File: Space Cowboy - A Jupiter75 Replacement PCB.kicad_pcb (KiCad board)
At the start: 2 copper layers, 313.5 x 129.5 mm, 237 parts, among them SW1 SW_PUSH, U1 ATmega32U4-AU, Y1 16MHz

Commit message: Update Space Cowboy - A Jupiter75 Replacement PCB.kicad_pcb
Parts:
- moved CRGB12 137.7 mm to (14.1, 43.7)
- moved CRGB6 119.2 mm to (161.1, 177.2)
- moved DRGB1 73.8 mm to (-24.5, 88.1)
- moved CRGB1 69.6 mm to (8.48, 49.6)
- moved CRGB2 62.9 mm to (-12.9, 54.4)
- moved DRGB17 61.6 mm to (92.9, 173.8)
- moved DRGB2 58.8 mm to (-11.5, 45.6)
- moved DRGB18 49.5 mm to (-2.03, 155.2)
- moved CRGB18 44.8 mm to (5.18, 153.3)
- moved DRGB9 37.3 mm to (321.4, 23.7)
- moved CRGB9 34.9 mm to (327.8, 20.7)
- moved DRGB11 31.7 mm to (379.3, 167.1)
- moved CRGB11 28.8 mm to (373.8, 162.9)
- moved DRGB10 23.2 mm to (371.3, 103.5)
- moved CRGB10 20.2 mm to (370.7, 111.8)
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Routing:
- net (no net): track 50.4 -> 0.00 mm
- net ROW5: track 272.3 -> 321.1 mm
- net +5V: track 294.4 -> 265.2 mm
- net GND: track 92.6 -> 68.7 mm
- net Net-(F1-Pad2): track 12.2 -> 4.56 mm
- net D+: track 21.7 -> 15.6 mm
- net D-: track 21.1 -> 15.4 mm
- net ROW4: track 278.7 -> 283.3 mm
- net Net-(R2-Pad2): track 192.5 -> 188.4 mm
- net Net-(R3-Pad1): track 193.2 -> 189.3 mm
- net Net-(D80-Pad2): track 28.8 -> 26.8 mm
- net Net-(R5-Pad1): track 3.84 -> 5.76 mm
- net Net-(FB2-Pad2): track 33.9 -> 35.4 mm
- net VBUS: track 20.2 -> 18.9 mm
- net COL0: track 152.5 -> 151.9 mm
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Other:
- board size 313.5 x 129.5 mm -> 303.5 x 119.5 mm

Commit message: Update Space Cowboy - A Jupiter75 Replacement PCB.kicad_pcb
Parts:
- moved D83 10.1 mm to (312.8, 152.4)
- moved D81 10.1 mm to (258.0, 152.4)
- moved D84 10.0 mm to (331.7, 152.4)
- moved D82 7.14 mm to (281.8, 152.4)
- moved D80 6.12 mm to (196.8, 146.3), turned to 270 degrees
- moved R7 3.71 mm to (138.7, 145.9)
- moved C3 3.57 mm to (157.2, 148.1)
- moved C1 3.56 mm to (142.0, 151.0)
- moved C4 3.51 mm to (142.0, 149.7)
- moved R1 3.43 mm to (158.5, 154.4)
- moved Y1 3.39 mm to (149.9, 141.0)
- moved U1 3.38 mm to (150.1, 151.2)
- moved D85 3.20 mm to (341.9, 156.5), turned to 0 degrees
- moved C6 3.01 mm to (153.3, 141.4)
- moved C7 3.01 mm to (146.4, 141.4)
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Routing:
- net ROW5: track 321.1 -> 290.0 mm
- net Net-(R2-Pad2): track 188.4 -> 173.6 mm
- net Net-(R3-Pad1): track 189.3 -> 174.7 mm
- net +5V: track 265.2 -> 268.7 mm
- net Net-(D85-Pad2): track 11.4 -> 9.31 mm
- net GND: track 68.7 -> 66.7 mm
- net Net-(D80-Pad2): track 26.8 -> 25.6 mm
- net Net-(D84-Pad2): track 10.8 -> 9.64 mm
- net Net-(D81-Pad2): track 10.8 -> 9.75 mm
- net Net-(D83-Pad2): track 10.8 -> 9.79 mm

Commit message: Update Space Cowboy - A Jupiter75 Replacement PCB.kicad_pcb
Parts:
- moved DRGB18 143.9 mm to (141.0, 139.4), turned to 180 degrees
- moved DRGB1 137.5 mm to (103.0, 139.4), turned to 180 degrees
- moved DRGB2 121.1 mm to (65.0, 139.4), turned to 135 degrees
- moved DRGB17 92.8 mm to (179.0, 139.4), turned to 180 degrees
- moved DRGB14 66.7 mm to (293.0, 139.4), turned to 180 degrees
- moved DRGB15 64.1 mm to (255.0, 139.4), turned to 180 degrees
- moved DRGB13 63.1 mm to (331.1, 139.4), turned to 225 degrees
- moved DRGB16 56.9 mm to (217.0, 139.4), turned to 180 degrees
- moved C6 20.0 mm to (134.4, 148.0), turned to 0 degrees
- moved Y1 18.7 mm to (134.3, 151.4), turned to 270 degrees
- moved C7 18.0 mm to (134.4, 154.8), turned to 0 degrees
- moved C8 16.6 mm to (136.5, 158.2), turned to 90 degrees
- moved C5 16.3 mm to (162.2, 154.8), turned to 270 degrees
- moved R7 14.1 mm to (142.2, 159.6), turned to 90 degrees
- moved C2 13.4 mm to (162.2, 147.5), turned to 270 degrees
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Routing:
- net +5V: track 268.7 -> 179.1 mm, vias 7 -> 2
- net GND: track 66.7 -> 9.08 mm, vias 2 -> 0
- net Net-(C7-Pad1): track 12.2 -> 0.82 mm
- net ROW4: track 283.3 -> 276.4 mm
- net Net-(C6-Pad2): track 8.79 -> 14.7 mm
- net ROW5: track 290.0 -> 284.3 mm
- net Net-(R1-Pad1): track 5.08 -> 0.00 mm
- net Net-(D70-Pad2): track 10.8 -> 13.1 mm
- net Net-(D68-Pad2): track 10.8 -> 13.1 mm
- net Net-(D64-Pad2): track 10.8 -> 13.1 mm
- net Net-(D72-Pad2): track 10.8 -> 13.1 mm
- net Net-(D66-Pad2): track 10.8 -> 13.0 mm
- net Net-(R7-Pad2): track 8.93 -> 6.99 mm
- net Net-(D63-Pad2): track 13.1 -> 11.5 mm

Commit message: Update Space Cowboy - A Jupiter75 Replacement PCB.kicad_pcb
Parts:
- moved CRGB13 332.8 mm to (328.4, 136.8), turned to 45 degrees
- moved CRGB12 323.4 mm to (331.0, 108.5), turned to 180 degrees
- moved CRGB14 301.2 mm to (291.9, 135.6)
- moved CRGB15 254.2 mm to (255.0, 135.7)
- moved CRGB16 221.5 mm to (217.0, 135.7)
- moved CRGB8 213.0 mm to (217.0, 73.8), turned to 180 degrees
- moved CRGB17 188.4 mm to (179.0, 135.7)
- moved CRGB7 178.4 mm to (179.1, 73.8), turned to 180 degrees
- moved CRGB4 144.9 mm to (62.4, 67.5), turned to 225 degrees
- moved CRGB18 137.0 mm to (141.0, 135.7), turned to 0 degrees
- moved CRGB1 127.9 mm to (103.0, 135.7), turned to 0 degrees
- moved CRGB5 125.4 mm to (103.0, 73.8), turned to 180 degrees
- moved CRGB2 115.6 mm to (62.4, 142.1), turned to 315 degrees
- moved DRGB11 108.4 mm to (331.0, 70.1), turned to 315 degrees
- moved CRGB6 105.4 mm to (141.1, 73.8), turned to 180 degrees
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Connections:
- DRGB1 pad 4DIN: (no net) -> RGB_DI_PIN
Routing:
- net +5V: track 179.1 -> 1045.2 mm, vias 2 -> 8
- net (no net): track 0.00 -> 588.0 mm, vias 0 -> 8
- net GND: track 9.08 -> 66.7 mm
- net ROW2: track 282.6 -> 276.8 mm
- net Net-(D33-Pad2): track 10.8 -> 15.2 mm
- net COL2: track 121.7 -> 123.8 mm
- net Net-(D46-Pad2): track 5.14 -> 3.70 mm

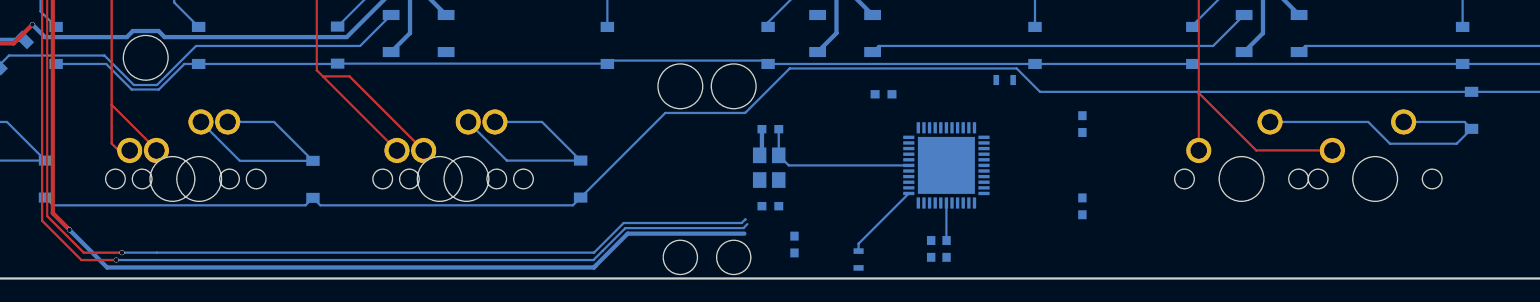
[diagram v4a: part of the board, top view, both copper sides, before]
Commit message: Update Space Cowboy - A Jupiter75 Replacement PCB.kicad_pcb
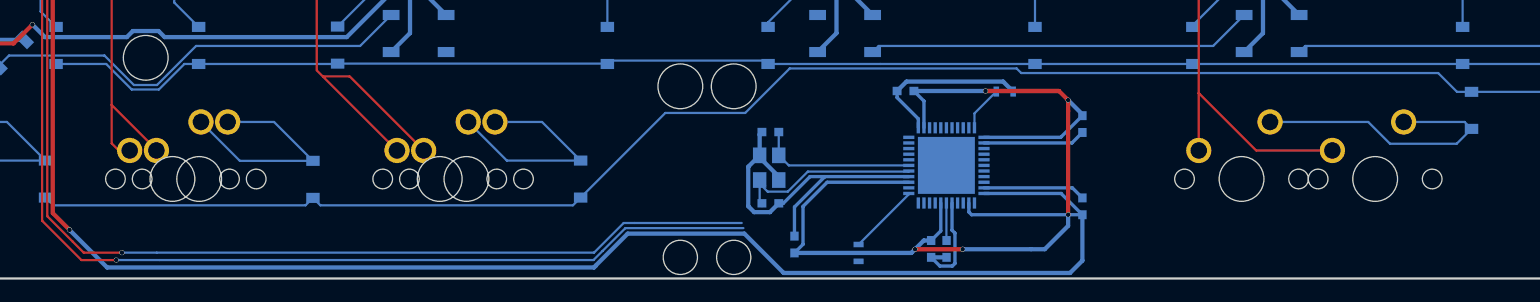
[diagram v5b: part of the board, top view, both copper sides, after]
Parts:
- moved C3 1.98 mm to (146.4, 144.6)
- moved R1 1.03 mm to (155.3, 144.6)
- moved R7 0.58 mm to (142.2, 159.0)
- moved C6 0.25 mm to (134.4, 148.2)
- moved C7 0.25 mm to (134.4, 154.6)
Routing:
- net +5V: track 1045.2 -> 1187.9 mm, vias 8 -> 13
- net GND: track 66.7 -> 139.7 mm
- net Net-(C7-Pad1): track 0.82 -> 18.0 mm
- net Net-(R1-Pad1): track 0.00 -> 4.03 mm
- net Net-(R7-Pad2): track 6.99 -> 6.40 mm
- net Net-(R3-Pad1): track 174.7 -> 174.2 mm

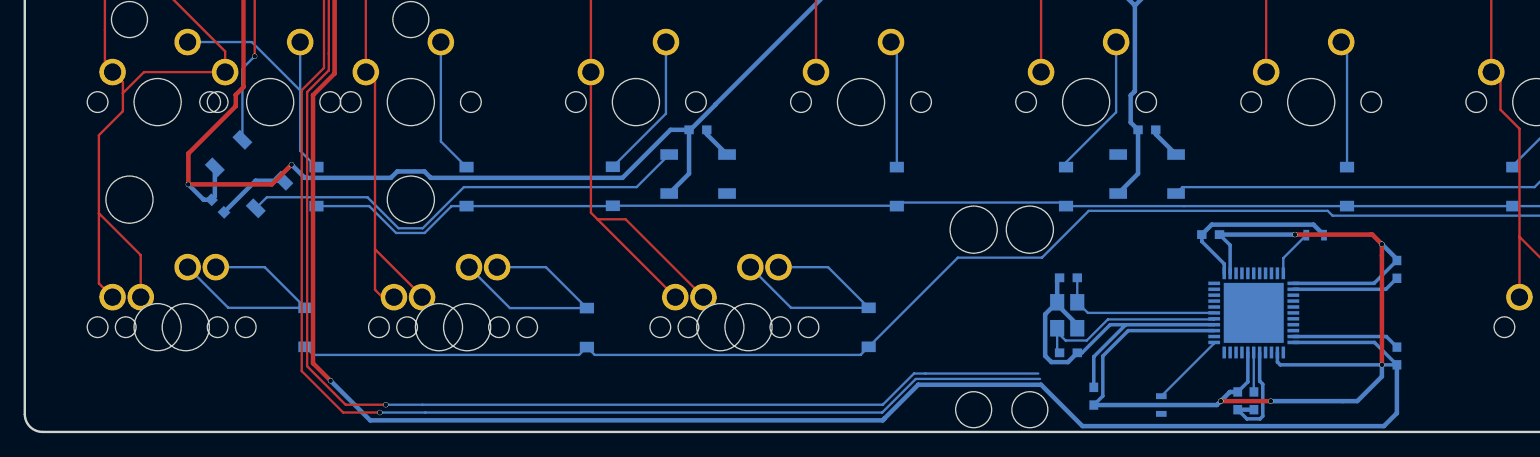
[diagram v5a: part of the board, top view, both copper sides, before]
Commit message: Update Space Cowboy - A Jupiter75 Replacement PCB.kicad_pcb
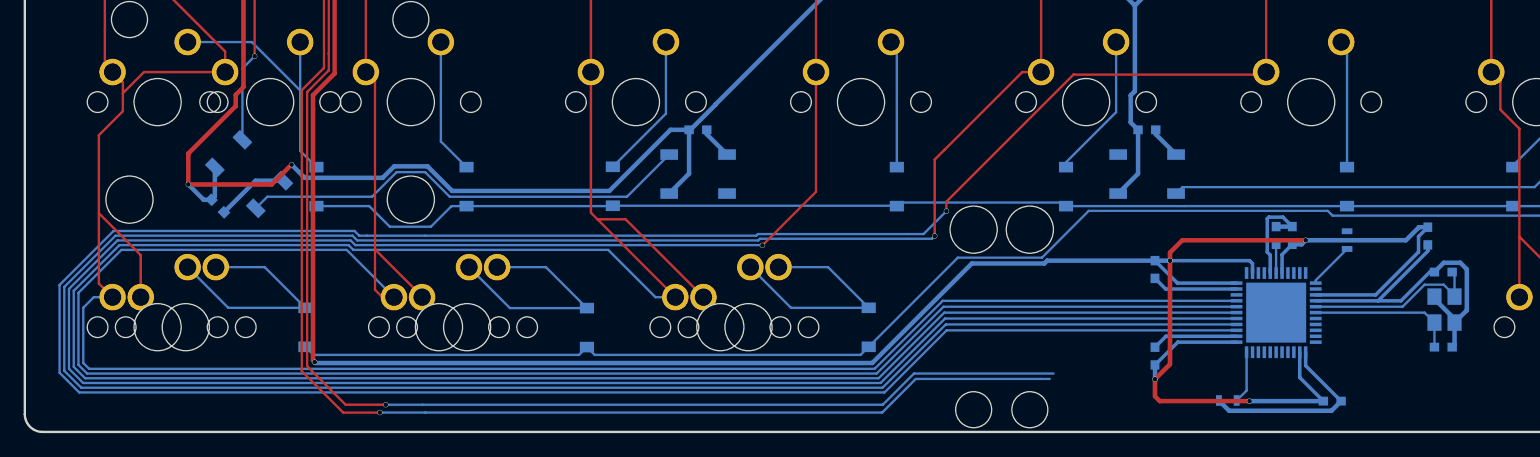
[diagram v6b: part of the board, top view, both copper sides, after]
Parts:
- moved C7 32.5 mm to (166.1, 147.7), turned to 180 degrees
- moved C6 32.3 mm to (166.1, 154.1), turned to 180 degrees
- moved Y1 31.9 mm to (166.2, 150.9), turned to 90 degrees
- moved C8 31.4 mm to (164.8, 144.7), turned to 270 degrees
- moved C2 21.7 mm to (141.7, 154.8), turned to 90 degrees
- moved C5 21.7 mm to (141.7, 147.5), turned to 90 degrees
- moved R7 21.0 mm to (158.0, 145.0), turned to 270 degrees
- moved C3 17.5 mm to (156.7, 158.6), turned to 0 degrees
- moved R1 15.8 mm to (147.9, 158.6), turned to 180 degrees
- moved C4 14.7 mm to (153.3, 144.6), turned to 90 degrees
- moved C1 14.1 mm to (152.0, 144.6), turned to 270 degrees
- moved U1 1.89 mm to (152.0, 151.2), turned to 270 degrees
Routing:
- net COL5: track 91.0 -> 311.3 mm, vias 0 -> 1
- net COL4: track 89.0 -> 292.5 mm, vias 0 -> 1
- net COL3: track 89.2 -> 274.6 mm, vias 0 -> 1
- net COL2: track 123.8 -> 285.7 mm
- net COL1: track 115.4 -> 252.0 mm
- net COL0: track 151.9 -> 259.6 mm
- net +5V: track 1187.9 -> 1153.6 mm, vias 13 -> 12
- net GND: track 139.7 -> 135.4 mm
- net Net-(R7-Pad2): track 6.40 -> 3.99 mm
- net Net-(C6-Pad2): track 14.4 -> 12.9 mm
- net Net-(C7-Pad1): track 18.0 -> 16.6 mm
- net Net-(R2-Pad2): track 173.1 -> 174.4 mm
- net Net-(C1-Pad2): track 3.56 -> 2.67 mm
- net Net-(R3-Pad1): track 174.2 -> 175.0 mm

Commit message: Update Space Cowboy - A Jupiter75 Replacement PCB.kicad_pcb
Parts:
- moved C3 1.98 mm to (156.7, 156.7)
- moved R1 1.93 mm to (147.9, 156.7)
- moved C2 0.38 mm to (141.7, 154.5)
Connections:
- U1 pad 21: COL15 -> COL6
- U1 pad 22: COL14 -> COL7
- U1 pad 25: COL13 -> COL8
- U1 pad 26: COL12 -> COL9
- U1 pad 27: COL11 -> COL10
- U1 pad 28: COL10 -> COL11
- U1 pad 29: COL9 -> COL12
- U1 pad 30: COL8 -> COL13
- U1 pad 31: COL7 -> COL14
- U1 pad 32: COL6 -> COL15
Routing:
- net COL15: track 97.6 -> 304.4 mm
- net COL14: track 103.6 -> 278.5 mm
- net COL12: track 119.0 -> 288.9 mm, vias 0 -> 1
- net COL13: track 130.7 -> 285.6 mm
- net COL11: track 129.9 -> 257.8 mm, vias 0 -> 2
- net COL10: track 114.6 -> 212.1 mm
- net COL9: track 93.0 -> 186.5 mm, vias 0 -> 2
- net COL8: track 91.0 -> 168.0 mm, vias 0 -> 2
- net COL7: track 91.0 -> 148.2 mm, vias 0 -> 2
- net COL6: track 125.2 -> 169.9 mm
- net +5V: track 1153.6 -> 1139.8 mm
- net COL2: track 285.7 -> 295.4 mm
- net COL0: track 259.6 -> 266.6 mm
- net COL1: track 252.0 -> 258.0 mm
- net Net-(R4-Pad1): track 0.00 -> 4.32 mm
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
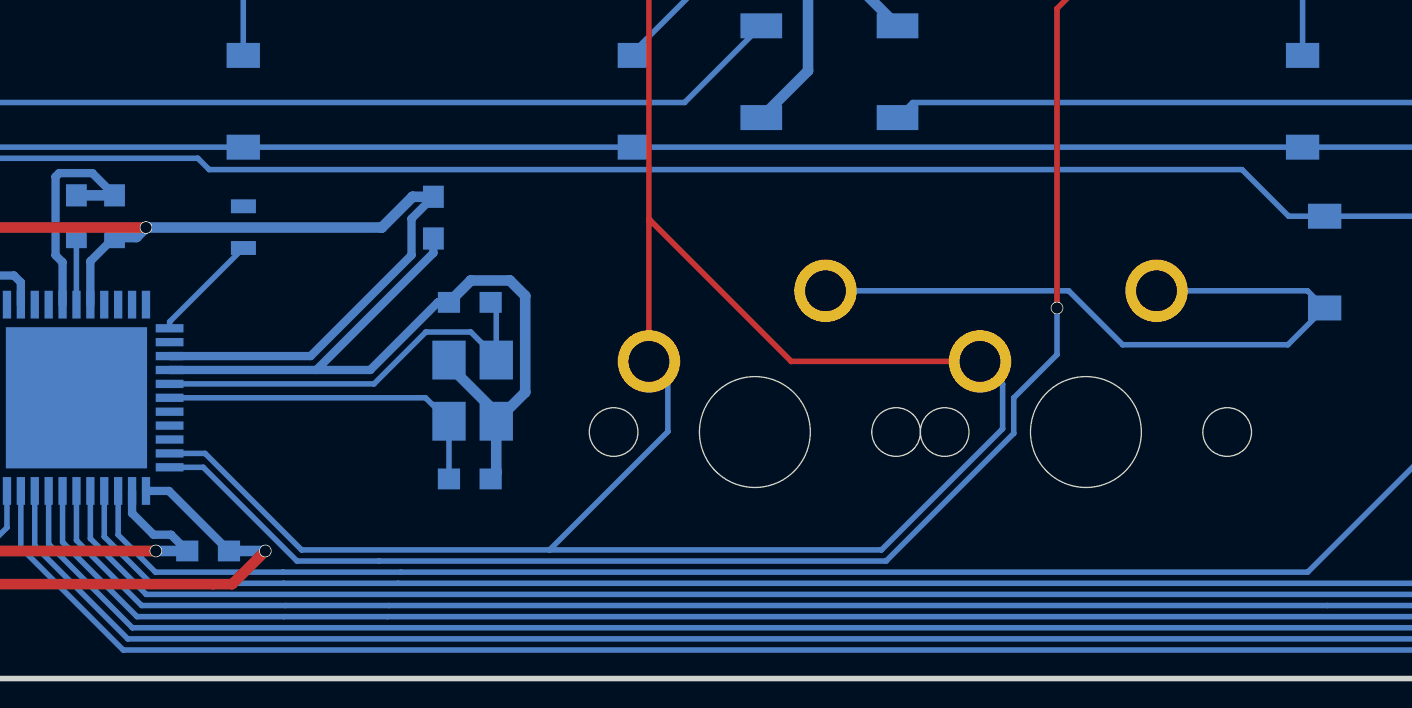
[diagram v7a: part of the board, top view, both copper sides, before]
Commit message: Update Space Cowboy - A Jupiter75 Replacement PCB.kicad_pcb
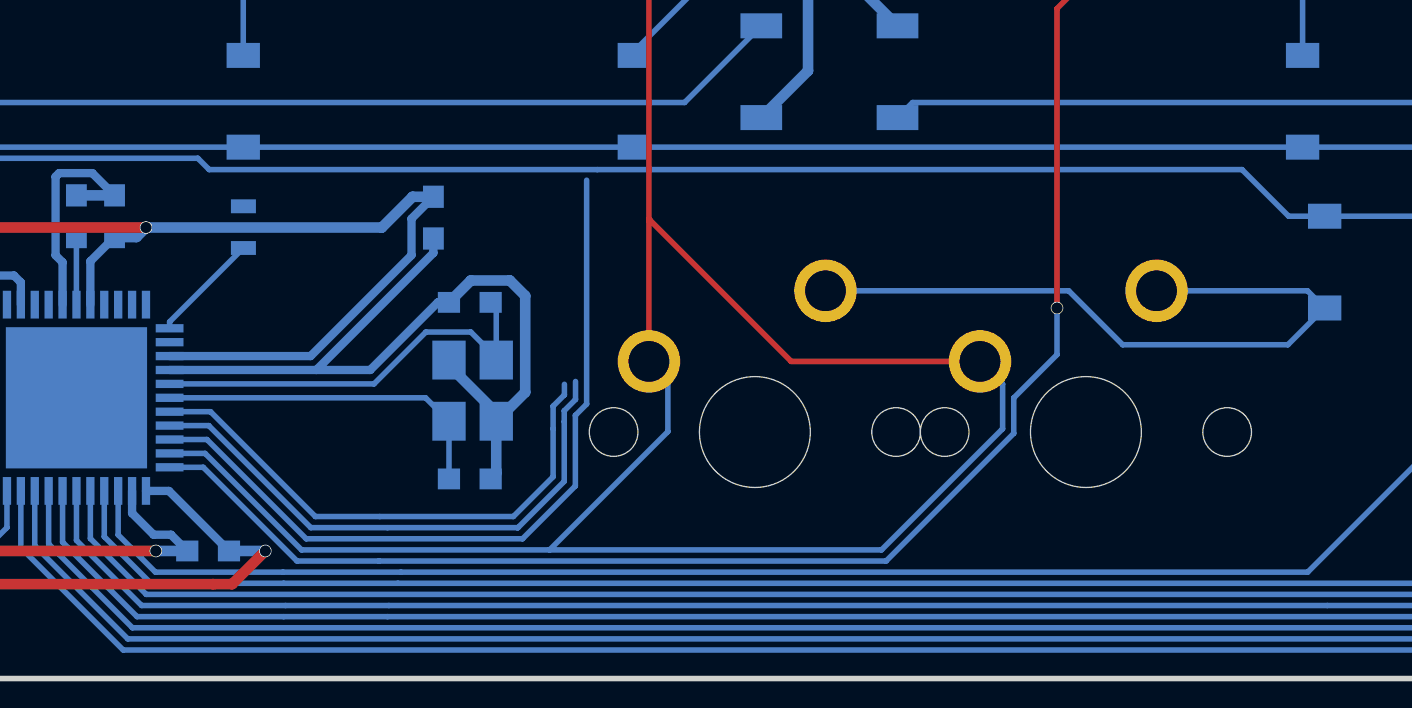
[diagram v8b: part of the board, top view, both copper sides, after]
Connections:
- U1 pad 10: ROW4 -> ROW1
- U1 pad 11: ROW3 -> ROW2
- U1 pad 18: ROW2 -> ROW3
- U1 pad 19: ROW1 -> ROW4
- U1 pad 20: ROW0 -> ROW5
- U1 pad 9: ROW5 -> ROW0
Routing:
- net ROW5: track 284.4 -> 312.4 mm
- net ROW4: track 276.3 -> 296.5 mm
- net ROW3: track 276.6 -> 296.0 mm
